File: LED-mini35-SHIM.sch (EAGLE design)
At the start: 19 parts, among them IC1 TXB0101DCKR

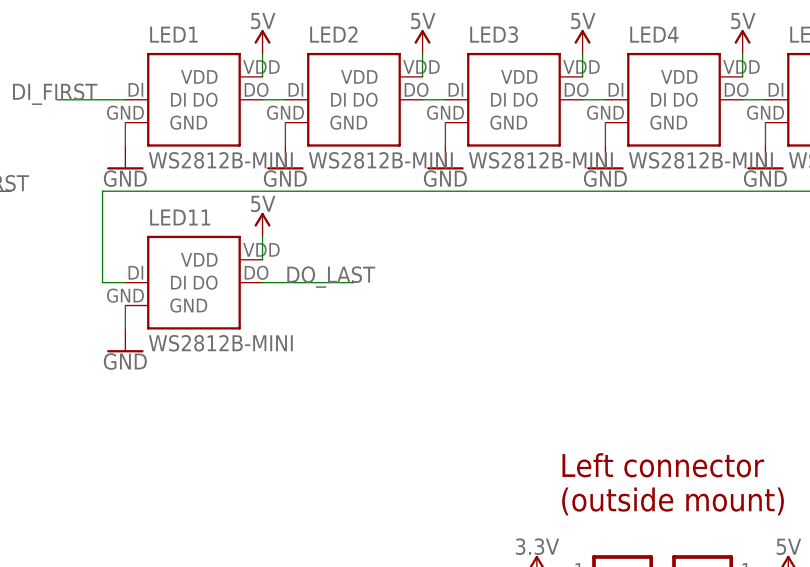
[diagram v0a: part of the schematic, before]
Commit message: Added one more 35mm LED to the mini-board. Generated CAM files. Generated PDF schematics. Generated PNG preview.
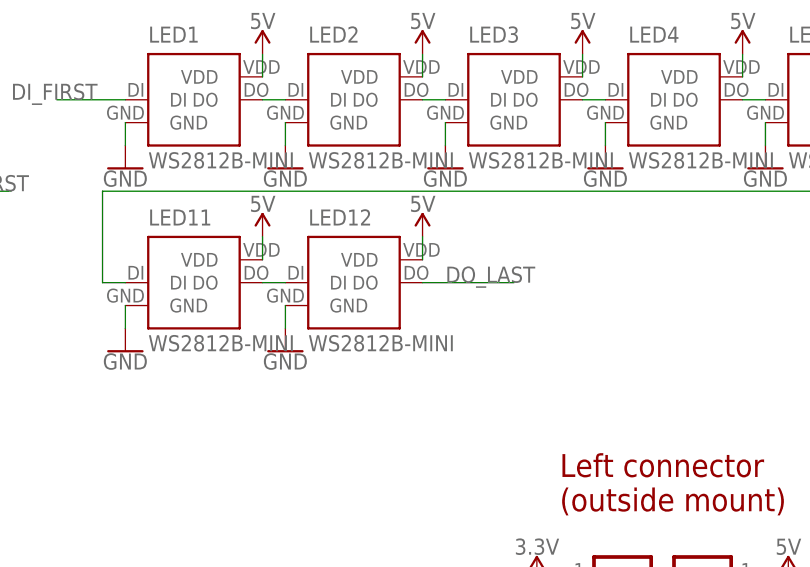
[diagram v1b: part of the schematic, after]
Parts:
- added LED12: WS2812B-MINI, WS281X:WS2812B-MINI
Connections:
- new net N$11: LED11.DO, LED12.DI
- net 5V: now also LED12.VDD
- net DO_LAST: now also LED12.DO; no longer LED11.DO
- net GND: now also LED12.GND
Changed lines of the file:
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@@
 <part name="SJ1" library="_my_jumpers" deviceset="SJ3" device=""/>
 <part name="LOGO1" library="_my_logos" deviceset="MFDECLOGO" device="_L_10MM" value="MFDECLOGO_L_10MM"/>
+<part name="LED12" library="WS281X" deviceset="WS2812" device="B-MINI" value="WS2812B-MINI"/>
+<part name="SUPPLY15" library="SparkFun-PowerSymbols" library_urn="urn:adsk.eagle:library:530" deviceset="5V" device=""/>
+<part name="GND14" library="SparkFun-PowerSymbols" library_urn="urn:adsk.eagle:library:530" deviceset="GND" device=""/>
 </parts>
 <sheets>
@@
 </instance>
 <instance part="LOGO1" gate="G$1" x="134.62" y="2.54" smashed="yes"/>
+<instance part="LED12" gate="LED" x="96.52" y="132.08" smashed="yes">
+<attribute name="NAME" x="91.44" y="138.43" size="1.778" layer="95"/>
+<attribute name="VALUE" x="91.44" y="124.46" size="1.778" layer="95"/>
+</instance>
+<instance part="SUPPLY15" gate="G$1" x="104.14" y="137.16" smashed="yes">
+<attribute name="VALUE" x="104.14" y="139.954" size="1.778" layer="96" align="bottom-center"/>
+</instance>
+<instance part="GND14" gate="1" x="88.9" y="124.46" smashed="yes">
+<attribute name="VALUE" x="88.9" y="124.206" size="1.778" layer="96" align="top-center"/>
+</instance>
 </instances>
 <busses>
@@
 <pinref part="GND149" gate="1" pin="GND"/>
 </segment>
+<segment>
+<pinref part="LED12" gate="LED" pin="GND"/>
+<pinref part="GND14" gate="1" pin="GND"/>
+<wire x1="88.9" y1="129.54" x2="88.9" y2="127" width="0.1524" layer="91"/>
+</segment>
 </net>
 <net name="GPIO2" class="0">
@@
 <pinref part="SUPPLY152" gate="G$1" pin="5V"/>
 </segment>
+<segment>
+<pinref part="LED12" gate="LED" pin="VDD"/>
+<pinref part="SUPPLY15" gate="G$1" pin="5V"/>
+<wire x1="104.14" y1="134.62" x2="104.14" y2="137.16" width="0.1524" layer="91"/>
+</segment>
 </net>
 <net name="N$1" class="0">
@@
 </segment>
 </net>
-<net name="DO_LAST" class="0">
-<segment>
-<wire x1="86.36" y1="132.08" x2="96.52" y2="132.08" width="0.1524" layer="91"/>
-<label x="88.9" y="132.08" size="1.778" layer="95"/>
-<pinref part="LED11" gate="LED" pin="DO"/>
-</segment>
-</net>
 <net name="DATA" class="0">
 <segment>
@@
 </segment>
 </net>
+<net name="N$11" class="0">
+<segment>
+<pinref part="LED12" gate="LED" pin="DI"/>
+<pinref part="LED11" gate="LED" pin="DO"/>
+<wire x1="88.9" y1="132.08" x2="86.36" y2="132.08" width="0.1524" layer="91"/>
+</segment>
+</net>
+<net name="DO_LAST" class="0">
+<segment>
+<pinref part="LED12" gate="LED" pin="DO"/>
+<wire x1="104.14" y1="132.08" x2="114.3" y2="132.08" width="0.1524" layer="91"/>
+<label x="106.68" y="132.08" size="1.778" layer="95"/>
+</segment>
+</net>
